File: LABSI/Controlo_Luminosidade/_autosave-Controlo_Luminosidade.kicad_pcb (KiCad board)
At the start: 2 copper layers, 60 x 80 mm, 41 parts, among them J1 5V/4A, J10 Touch Button, J11 Touch Button, J12 Touch Button, J2 Barrel_Jack_Switch, J3 Conn_01x05_Pin, J4 Conn_01x04_Pin, J5 Conn_01x04_Pin, J6 AVR-ISP-6, J7 Conn_01x03_Pin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

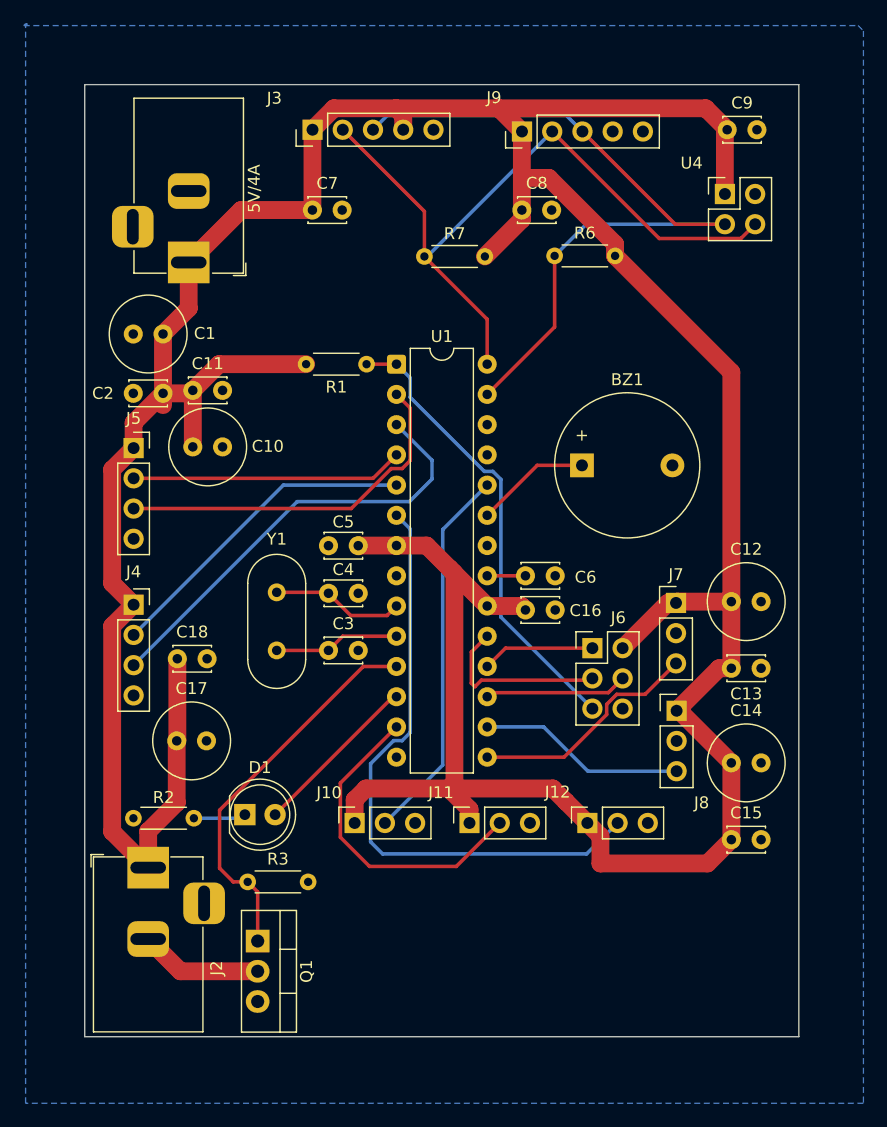
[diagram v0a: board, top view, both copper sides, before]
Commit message: sonar not working, integration with esp32 iot,
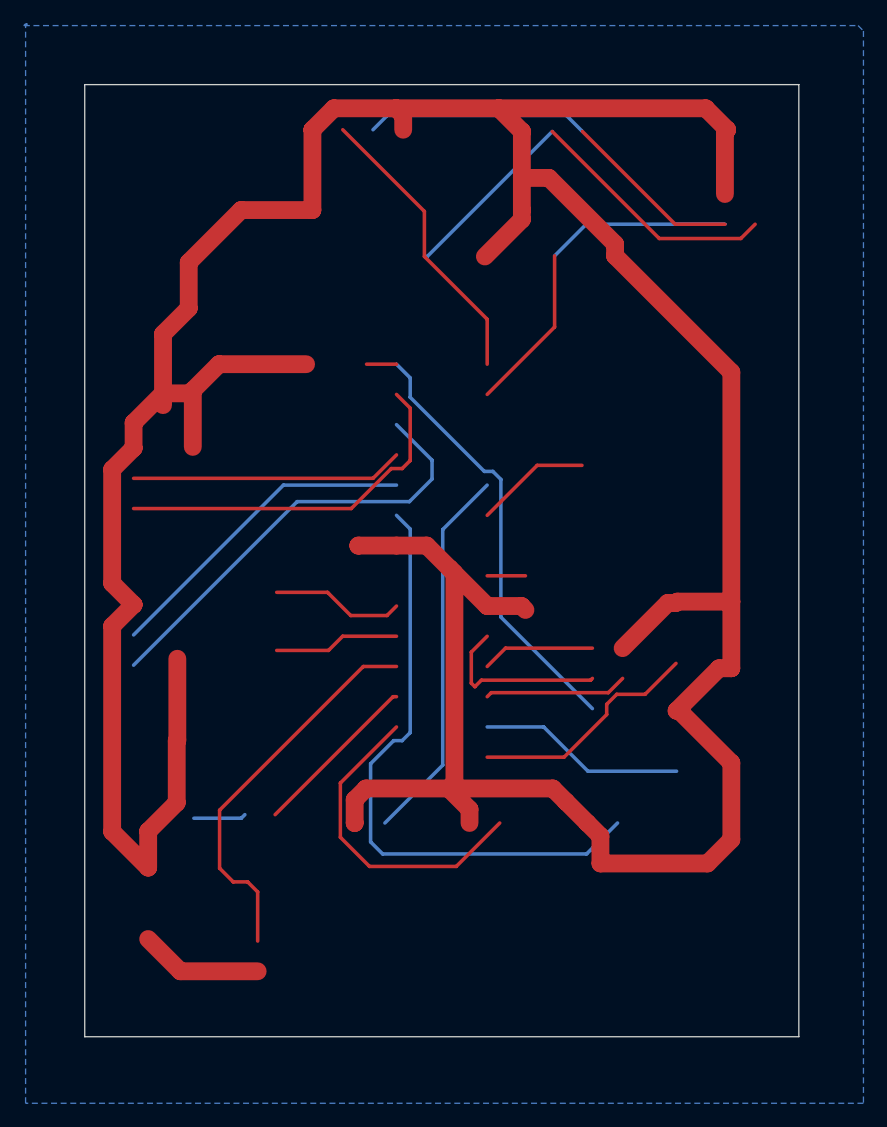
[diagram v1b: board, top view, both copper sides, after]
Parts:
- removed BZ1: Buzzer, Buzzer_Beeper:Buzzer_12x9.5RM7.6
- removed C1, C12, C14: 100u, Capacitor_THT:C_Radial_D6.3mm_H11.0mm_P2.50mm
- removed C10, C17: 10u, Capacitor_THT:C_Radial_D6.3mm_H11.0mm_P2.50mm
- removed C11, C13, C15, C16, C18, C2, C5, C6, C7, C8, C9: 0.1u, Capacitor_THT:C_Disc_D3.0mm_W2.0mm_P2.50mm
- removed C3, C4: 22p, Capacitor_THT:C_Disc_D3.0mm_W2.0mm_P2.50mm
- removed D1: GREEN-LED, LED_THT:LED_D5.0mm
- removed J1: 5V/4A, Connector_BarrelJack:BarrelJack_Horizontal
- removed J10, J11, J12: Touch Button, Connector_PinSocket_2.54mm:PinSocket_1x03_P2.54mm_Vertical
- removed J2: Barrel_Jack_Switch, Connector_BarrelJack:BarrelJack_Horizontal
- removed J3, J9: Conn_01x05_Pin, Connector_PinHeader_2.54mm:PinHeader_1x05_P2.54mm_Vertical
- removed J4, J5: Conn_01x04_Pin, Connector_PinSocket_2.54mm:PinSocket_1x04_P2.54mm_Vertical
- removed J6: AVR-ISP-6, Connector_PinHeader_2.54mm:PinHeader_2x03_P2.54mm_Vertical
- removed J7, J8: Conn_01x03_Pin, Connector_PinHeader_2.54mm:PinHeader_1x03_P2.54mm_Vertical
- removed Q1: IRLZ24, Package_TO_SOT_THT:TO-220-3_Vertical
- removed R1, R3, R6, R7: 10k, Resistor_THT:R_Axial_DIN0204_L3.6mm_D1.6mm_P5.08mm_Horizontal
- removed R2: 220, Resistor_THT:R_Axial_DIN0204_L3.6mm_D1.6mm_P5.08mm_Horizontal
- removed U1: ATmega328-P, Package_DIP:DIP-28_W7.62mm
- removed U4: I2C_4PIN, Connector_PinHeader_2.54mm:PinHeader_2x02_P2.54mm_Vertical
- removed Y1: 16M, Crystal:Crystal_HC49-4H_Vertical
